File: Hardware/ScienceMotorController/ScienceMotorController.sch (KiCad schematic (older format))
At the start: 0 parts

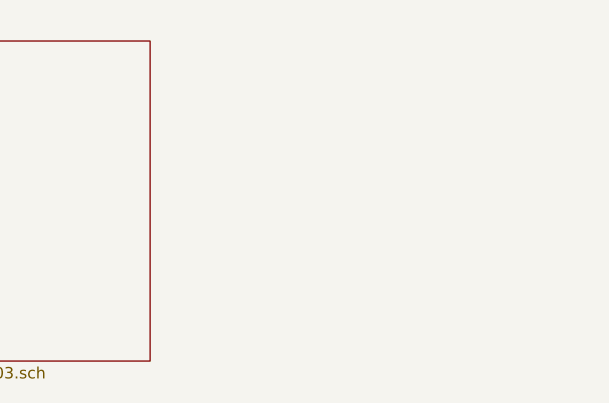
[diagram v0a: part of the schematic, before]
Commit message: Set up VNH IC's
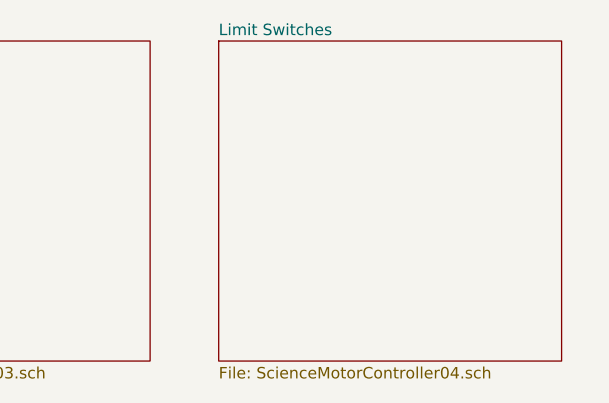
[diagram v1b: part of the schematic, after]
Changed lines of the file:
@@
 $Descr A 11000 8500
 encoding utf-8
-Sheet 1 4
+Sheet 1 10
 Title ""
 Date ""
@@
 F1 "ScienceMotorController03.sch" 50
 $EndSheet
+$Sheet
+S 6600 1050 1500 1400
+U 5F81B171
+F0 "Limit Switches" 50
+F1 "ScienceMotorController04.sch" 50
+$EndSheet
 $EndSCHEMATC

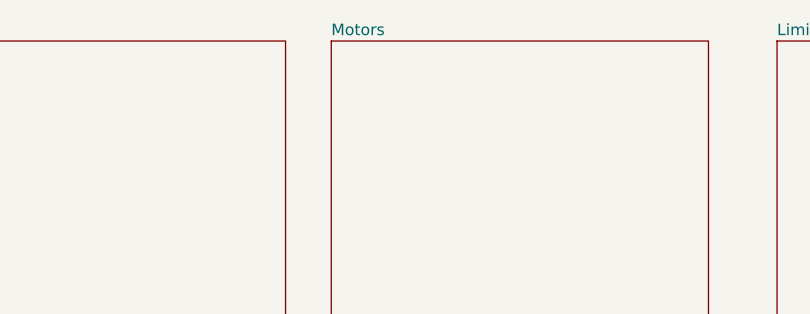
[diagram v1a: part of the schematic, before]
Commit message: Sheet titles
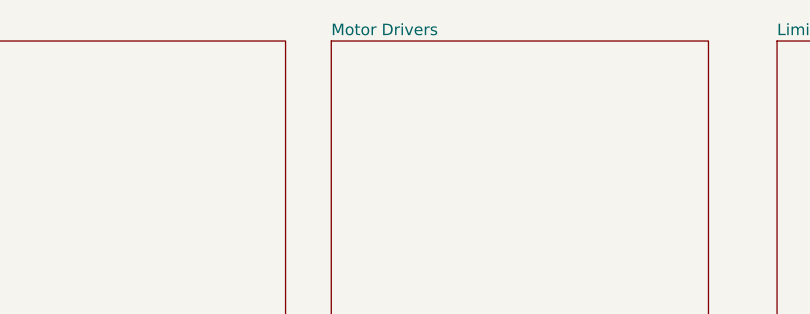
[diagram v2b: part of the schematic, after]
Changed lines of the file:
@@
 $Descr A 11000 8500
 encoding utf-8
-Sheet 1 10
+Sheet 1 11
 Title ""
 Date ""
@@
 S 4650 1050 1650 1400
 U 5F7D111E
-F0 "Motors" 50
+F0 "Motor Drivers" 50
 F1 "ScienceMotorController03.sch" 50
 $EndSheet

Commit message: schematic review
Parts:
- added Conn? (x2): AndersonPP, symbol MRDT_Connectors:AndersonPP
- added D?: LED, symbol Device:LED
- added R?: 1.2k, symbol Device:R_Small
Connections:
- new net: D?.2 (A), R?.1
- new net +12VA: Conn?.3 (V+Act), R?.2
- new net GND: Conn?.1 (GND), D?.1 (K)
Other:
- note added: "Orange"
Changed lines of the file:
@@
 $Descr A 11000 8500
 encoding utf-8
-Sheet 1 11
+Sheet 1 10
 Title ""
 Date ""
@@
 $EndDescr
 $Sheet
-S 1100 1050 1600 1400
+S 2500 900  1600 1400
 U 5F6E1E86
 F0 "Power" 50
 F1 "ScienceMotorController01.sch" 50
+F2 "12VA" I L 2500 1050 50
+F3 "3.3VA" O R 4100 1050 50
 $EndSheet
 $Sheet
-S 2800 1050 1650 1400
+S 4350 900  1650 1400
 U 5F7148FA
 F0 "Tiva" 39
 F1 "ScienceMotorController02.sch" 39
+F2 "3.3VA" I L 4350 1050 50
 $EndSheet
 $Sheet
-S 4650 1050 1650 1400
-U 5F7D111E
-F0 "Motor Drivers" 50
-F1 "ScienceMotorController03.sch" 50
-$EndSheet
-$Sheet
-S 6600 1050 1500 1400
+S 8100 900  1500 1400
 U 5F81B171
 F0 "Limit Switches" 50
 F1 "ScienceMotorController04.sch" 50
 $EndSheet
+$Comp
+L MRDT_Connectors:AndersonPP Conn?
+U 3 1 5F8E3C0A
+P 650 1400
+AR Path="/5F6E1E86/5F8E3C0A" Ref="Conn?"  Part="3"
+AR Path="/5F8E3C0A" Ref="Conn?"  Part="3"
+F 0 "Conn?" H 858 1787 60  0000 C CNN
+F 1 "AndersonPP" H 858 1681 60  0000 C CNN
+F 2 "" H 500 850 60  0001 C CNN
+F 3 "" H 500 850 60  0001 C CNN
+	3    650  1400
+	1    0    0    -1
+$EndComp
+Wire Wire Line
+	1050 1300 1200 1300
+$Comp
+L power:+12VA #PWR?
+U 1 1 5F8E3C12
+P 1200 1000
+AR Path="/5F6E1E86/5F8E3C12" Ref="#PWR?"  Part="1"
+AR Path="/5F8E3C12" Ref="#PWR?"  Part="1"
+F 0 "#PWR?" H 1200 850 50  0001 C CNN
+F 1 "+12VA" H 1215 1173 50  0000 C CNN
+F 2 "" H 1200 1000 50  0001 C CNN
+F 3 "" H 1200 1000 50  0001 C CNN
+	1    1200 1000
+	1    0    0    -1
+$EndComp
+$Comp
+L Device:LED D?
+U 1 1 5F8E3C18
+P 1700 1400
+AR Path="/5F6E1E86/5F8E3C18" Ref="D?"  Part="1"
+AR Path="/5F8E3C18" Ref="D?"  Part="1"
+F 0 "D?" H 1700 1200 50  0000 C CNN
+F 1 "LED" H 1700 1300 50  0000 C CNN
+F 2 "" H 1700 1400 50  0001 C CNN
+F 3 "~" H 1700 1400 50  0001 C CNN
+	1    1700 1400
+	-1   0    0    1
+$EndComp
+Wire Wire Line
+	1200 1400 1200 1300
+Connection ~ 1200 1300
+$Comp
+L Device:R_Small R?
+U 1 1 5F8E3C20
+P 1300 1400
+AR Path="/5F6E1E86/5F8E3C20" Ref="R?"  Part="1"
+AR Path="/5F8E3C20" Ref="R?"  Part="1"
+F 0 "R?" V 1104 1400 50  0000 C CNN
+F 1 "1.2k" V 1195 1400 50  0000 C CNN
+F 2 "" H 1300 1400 50  0001 C CNN
+F 3 "~" H 1300 1400 50  0001 C CNN
+	1    1300 1400
+	0    1    1    0
+$EndComp
+Wire Wire Line
+	1400 1400 1550 1400
+$Comp
+L power:GND #PWR?
+U 1 1 5F8E3C27
+P 1950 1450
+AR Path="/5F6E1E86/5F8E3C27" Ref="#PWR?"  Part="1"
+AR Path="/5F8E3C27" Ref="#PWR?"  Part="1"
+F 0 "#PWR?" H 1950 1200 50  0001 C CNN
+F 1 "GND" H 1955 1277 50  0000 C CNN
+F 2 "" H 1950 1450 50  0001 C CNN
+F 3 "" H 1950 1450 50  0001 C CNN
+	1    1950 1450
+	1    0    0    -1
+$EndComp
+Wire Wire Line
+	1850 1400 1950 1400
+Wire Wire Line
+	1950 1400 1950 1450
+Text Notes 1600 1500 0    50   ~ 0
+Orange
+Wire Wire Line
+	1200 1050 1200 1300
+Wire Wire Line
+	2500 1050 1200 1050
+Connection ~ 1200 1050
+Wire Wire Line
+	1200 1000 1200 1050
+$Comp
+L MRDT_Connectors:AndersonPP Conn?
+U 1 1 5F8FDE30
+P 600 2100
+AR Path="/5F6E1E86/5F8FDE30" Ref="Conn?"  Part="1"
+AR Path="/5F8FDE30" Ref="Conn?"  Part="1"
+F 0 "Conn?" H 808 2487 60  0000 C CNN
+F 1 "AndersonPP" H 808 2381 60  0000 C CNN
+F 2 "" H 450 1550 60  0001 C CNN
+F 3 "" H 450 1550 60  0001 C CNN
+	1    600  2100
+	1    0    0    -1
+$EndComp
+$Comp
+L power:GND #PWR?
+U 1 1 5F8FDE36
+P 1150 2200
+AR Path="/5F6E1E86/5F8FDE36" Ref="#PWR?"  Part="1"
+AR Path="/5F8FDE36" Ref="#PWR?"  Part="1"
+F 0 "#PWR?" H 1150 1950 50  0001 C CNN
+F 1 "GND" H 1155 2027 50  0000 C CNN
+F 2 "" H 1150 2200 50  0001 C CNN
+F 3 "" H 1150 2200 50  0001 C CNN
+	1    1150 2200
+	1    0    0    -1
+$EndComp
+Wire Wire Line
+	1150 2200 1150 2000
+Wire Wire Line
+	1150 2000 1000 2000
+Wire Wire Line
+	4100 1050 4350 1050
+$Sheet
+S 2500 3150 1450 1300
+U 5F9082F6
+F0 "sheet5F9082EF" 39
+F1 "ScienceMotorController03a.sch" 39
+$EndSheet
+$Sheet
+S 4050 3150 1400 1300
+U 5F9082F8
+F0 "sheet5F9082F0" 39
+F1 "ScienceMotorController03b.sch" 39
+$EndSheet
+$Sheet
+S 2500 4650 1450 1200
+U 5F9082FA
+F0 "sheet5F9082F1" 39
+F1 "ScienceMotorController03c.sch" 39
+$EndSheet
+$Sheet
+S 4050 4650 1400 1200
+U 5F9082FC
+F0 "sheet5F9082F2" 39
+F1 "ScienceMotorController03d.sch" 39
+$EndSheet
+$Sheet
+S 2500 6000 1450 1150
+U 5F9082FE
+F0 "sheet5F9082F3" 39
+F1 "ScienceMotorController03e.sch" 39
+$EndSheet
+$Sheet
+S 4050 6000 1400 1150
+U 5F908300
+F0 "sheet5F9082F4" 39
+F1 "ScienceMotorController03f.sch" 39
+$EndSheet
 $EndSCHEMATC

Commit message: made some more hierarchal changes
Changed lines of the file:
@@
 $EndSheet
 $Sheet
-S 8100 900  1500 1400
+S 4350 2500 1500 1400
 U 5F81B171
 F0 "Limit Switches" 50
 F1 "ScienceMotorController04.sch" 50
+F2 "3.3VA" I L 4350 2700 50
 $EndSheet
 $Comp
@@
 	1150 2000 1000 2000
 Wire Wire Line
-	4100 1050 4350 1050
+	4100 1050 4200 1050
 $Sheet
-S 2500 3150 1450 1300
+S 11700 3550 1450 1300
 U 5F9082F6
 F0 "sheet5F9082EF" 39
@@
 $EndSheet
 $Sheet
-S 4050 3150 1400 1300
+S 13250 3550 1400 1300
 U 5F9082F8
 F0 "sheet5F9082F0" 39
@@
 $EndSheet
 $Sheet
-S 2500 4650 1450 1200
+S 11700 5050 1450 1200
 U 5F9082FA
 F0 "sheet5F9082F1" 39
@@
 $EndSheet
 $Sheet
-S 4050 4650 1400 1200
+S 13250 5050 1400 1200
 U 5F9082FC
 F0 "sheet5F9082F2" 39
@@
 $EndSheet
 $Sheet
-S 2500 6000 1450 1150
+S 11700 6400 1450 1150
 U 5F9082FE
 F0 "sheet5F9082F3" 39
@@
 $EndSheet
 $Sheet
-S 4050 6000 1400 1150
+S 13250 6400 1400 1150
 U 5F908300
 F0 "sheet5F9082F4" 39
 F1 "ScienceMotorController03f.sch" 39
 $EndSheet
+Wire Wire Line
+	4350 2700 4200 2700
+Wire Wire Line
+	4200 2700 4200 1050
+Connection ~ 4200 1050
+Wire Wire Line
+	4200 1050 4350 1050
 $EndSCHEMATC

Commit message: fixed hierarchical
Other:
- moved on the sheet: Conn?A, Conn?C, D?, R?
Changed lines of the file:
@@
 $Descr A 11000 8500
 encoding utf-8
-Sheet 1 10
+Sheet 1 11
 Title ""
 Date ""
@@
 $EndDescr
 $Sheet
-S 2500 900  1600 1400
+S 4350 3300 1600 1400
 U 5F6E1E86
 F0 "Power" 50
 F1 "ScienceMotorController01.sch" 50
-F2 "12VA" I L 2500 1050 50
-F3 "3.3VA" O R 4100 1050 50
+F2 "12VA" I L 4350 3450 50
+F3 "3.3VA" O R 5950 3450 50
 $EndSheet
 $Sheet
-S 4350 900  1650 1400
+S 6200 3300 1650 1400
 U 5F7148FA
 F0 "Tiva" 39
 F1 "ScienceMotorController02.sch" 39
-F2 "3.3VA" I L 4350 1050 50
-$EndSheet
-$Sheet
-S 4350 2500 1500 1400
-U 5F81B171
-F0 "Limit Switches" 50
-F1 "ScienceMotorController04.sch" 50
-F2 "3.3VA" I L 4350 2700 50
+F2 "3.3VA" I L 6200 3450 50
 $EndSheet
 $Comp
 L MRDT_Connectors:AndersonPP Conn?
 U 3 1 5F8E3C0A
-P 650 1400
+P 2500 3800
 AR Path="/5F6E1E86/5F8E3C0A" Ref="Conn?"  Part="3"
 AR Path="/5F8E3C0A" Ref="Conn?"  Part="3"
-F 0 "Conn?" H 858 1787 60  0000 C CNN
-F 1 "AndersonPP" H 858 1681 60  0000 C CNN
-F 2 "" H 500 850 60  0001 C CNN
-F 3 "" H 500 850 60  0001 C CNN
-	3    650  1400
+F 0 "Conn?" H 2708 4187 60  0000 C CNN
+F 1 "AndersonPP" H 2708 4081 60  0000 C CNN
+F 2 "" H 2350 3250 60  0001 C CNN
+F 3 "" H 2350 3250 60  0001 C CNN
+	3    2500 3800
 	1    0    0    -1
 $EndComp
 Wire Wire Line
-	1050 1300 1200 1300
+	2900 3700 3050 3700
 $Comp
 L power:+12VA #PWR?
 U 1 1 5F8E3C12
-P 1200 1000
+P 3050 3400
 AR Path="/5F6E1E86/5F8E3C12" Ref="#PWR?"  Part="1"
 AR Path="/5F8E3C12" Ref="#PWR?"  Part="1"
-F 0 "#PWR?" H 1200 850 50  0001 C CNN
-F 1 "+12VA" H 1215 1173 50  0000 C CNN
-F 2 "" H 1200 1000 50  0001 C CNN
-F 3 "" H 1200 1000 50  0001 C CNN
-	1    1200 1000
+F 0 "#PWR?" H 3050 3250 50  0001 C CNN
+F 1 "+12VA" H 3065 3573 50  0000 C CNN
+F 2 "" H 3050 3400 50  0001 C CNN
+F 3 "" H 3050 3400 50  0001 C CNN
+	1    3050 3400
 	1    0    0    -1
 $EndComp
@@
 L Device:LED D?
 U 1 1 5F8E3C18
-P 1700 1400
+P 3550 3800
 AR Path="/5F6E1E86/5F8E3C18" Ref="D?"  Part="1"
 AR Path="/5F8E3C18" Ref="D?"  Part="1"
-F 0 "D?" H 1700 1200 50  0000 C CNN
-F 1 "LED" H 1700 1300 50  0000 C CNN
-F 2 "" H 1700 1400 50  0001 C CNN
-F 3 "~" H 1700 1400 50  0001 C CNN
-	1    1700 1400
+F 0 "D?" H 3550 3600 50  0000 C CNN
+F 1 "LED" H 3550 3700 50  0000 C CNN
+F 2 "" H 3550 3800 50  0001 C CNN
+F 3 "~" H 3550 3800 50  0001 C CNN
+	1    3550 3800
 	-1   0    0    1
 $EndComp
 Wire Wire Line
-	1200 1400 1200 1300
-Connection ~ 1200 1300
+	3050 3800 3050 3700
+Connection ~ 3050 3700
 $Comp
 L Device:R_Small R?
 U 1 1 5F8E3C20
-P 1300 1400
+P 3150 3800
 AR Path="/5F6E1E86/5F8E3C20" Ref="R?"  Part="1"
 AR Path="/5F8E3C20" Ref="R?"  Part="1"
-F 0 "R?" V 1104 1400 50  0000 C CNN
-F 1 "1.2k" V 1195 1400 50  0000 C CNN
-F 2 "" H 1300 1400 50  0001 C CNN
-F 3 "~" H 1300 1400 50  0001 C CNN
-	1    1300 1400
+F 0 "R?" V 2954 3800 50  0000 C CNN
+F 1 "1.2k" V 3045 3800 50  0000 C CNN
+F 2 "" H 3150 3800 50  0001 C CNN
+F 3 "~" H 3150 3800 50  0001 C CNN
+	1    3150 3800
 	0    1    1    0
 $EndComp
 Wire Wire Line
-	1400 1400 1550 1400
+	3250 3800 3400 3800
 $Comp
 L power:GND #PWR?
 U 1 1 5F8E3C27
-P 1950 1450
+P 3800 3850
 AR Path="/5F6E1E86/5F8E3C27" Ref="#PWR?"  Part="1"
 AR Path="/5F8E3C27" Ref="#PWR?"  Part="1"
-F 0 "#PWR?" H 1950 1200 50  0001 C CNN
-F 1 "GND" H 1955 1277 50  0000 C CNN
-F 2 "" H 1950 1450 50  0001 C CNN
-F 3 "" H 1950 1450 50  0001 C CNN
-	1    1950 1450
+F 0 "#PWR?" H 3800 3600 50  0001 C CNN
+F 1 "GND" H 3805 3677 50  0000 C CNN
+F 2 "" H 3800 3850 50  0001 C CNN
+F 3 "" H 3800 3850 50  0001 C CNN
+	1    3800 3850
 	1    0    0    -1
 $EndComp
 Wire Wire Line
-	1850 1400 1950 1400
+	3700 3800 3800 3800
 Wire Wire Line
-	1950 1400 1950 1450
-Text Notes 1600 1500 0    50   ~ 0
+	3800 3800 3800 3850
+Text Notes 3450 3900 0    50   ~ 0
 Orange
 Wire Wire Line
-	1200 1050 1200 1300
+	3050 3450 3050 3700
 Wire Wire Line
-	2500 1050 1200 1050
-Connection ~ 1200 1050
+	4350 3450 3050 3450
+Connection ~ 3050 3450
 Wire Wire Line
-	1200 1000 1200 1050
+	3050 3400 3050 3450
 $Comp
 L MRDT_Connectors:AndersonPP Conn?
 U 1 1 5F8FDE30
-P 600 2100
+P 2500 4300
 AR Path="/5F6E1E86/5F8FDE30" Ref="Conn?"  Part="1"
 AR Path="/5F8FDE30" Ref="Conn?"  Part="1"
-F 0 "Conn?" H 808 2487 60  0000 C CNN
-F 1 "AndersonPP" H 808 2381 60  0000 C CNN
-F 2 "" H 450 1550 60  0001 C CNN
-F 3 "" H 450 1550 60  0001 C CNN
-	1    600  2100
+F 0 "Conn?" H 2708 4687 60  0000 C CNN
+F 1 "AndersonPP" H 2708 4581 60  0000 C CNN
+F 2 "" H 2350 3750 60  0001 C CNN
+F 3 "" H 2350 3750 60  0001 C CNN
+	1    2500 4300
 	1    0    0    -1
 $EndComp
@@
 L power:GND #PWR?
 U 1 1 5F8FDE36
-P 1150 2200
+P 3050 4400
 AR Path="/5F6E1E86/5F8FDE36" Ref="#PWR?"  Part="1"
 AR Path="/5F8FDE36" Ref="#PWR?"  Part="1"
-F 0 "#PWR?" H 1150 1950 50  0001 C CNN
-F 1 "GND" H 1155 2027 50  0000 C CNN
-F 2 "" H 1150 2200 50  0001 C CNN
-F 3 "" H 1150 2200 50  0001 C CNN
-	1    1150 2200
+F 0 "#PWR?" H 3050 4150 50  0001 C CNN
+F 1 "GND" H 3055 4227 50  0000 C CNN
+F 2 "" H 3050 4400 50  0001 C CNN
+F 3 "" H 3050 4400 50  0001 C CNN
+	1    3050 4400
 	1    0    0    -1
 $EndComp
 Wire Wire Line
-	1150 2200 1150 2000
+	3050 4400 3050 4200
 Wire Wire Line
-	1150 2000 1000 2000
+	3050 4200 2900 4200
 Wire Wire Line
-	4100 1050 4200 1050
-$Sheet
-S 11700 3550 1450 1300
-U 5F9082F6
-F0 "sheet5F9082EF" 39
-F1 "ScienceMotorController03a.sch" 39
-$EndSheet
-$Sheet
-S 13250 3550 1400 1300
-U 5F9082F8
-F0 "sheet5F9082F0" 39
-F1 "ScienceMotorController03b.sch" 39
-$EndSheet
-$Sheet
-S 11700 5050 1450 1200
-U 5F9082FA
-F0 "sheet5F9082F1" 39
-F1 "ScienceMotorController03c.sch" 39
-$EndSheet
-$Sheet
-S 13250 5050 1400 1200
-U 5F9082FC
-F0 "sheet5F9082F2" 39
-F1 "ScienceMotorController03d.sch" 39
-$EndSheet
-$Sheet
-S 11700 6400 1450 1150
-U 5F9082FE
-F0 "sheet5F9082F3" 39
-F1 "ScienceMotorController03e.sch" 39
-$EndSheet
-$Sheet
-S 13250 6400 1400 1150
-U 5F908300
-F0 "sheet5F9082F4" 39
-F1 "ScienceMotorController03f.sch" 39
-$EndSheet
-Wire Wire Line
-	4350 2700 4200 2700
-Wire Wire Line
-	4200 2700 4200 1050
-Connection ~ 4200 1050
-Wire Wire Line
-	4200 1050 4350 1050
+	5950 3450 6200 3450
 $EndSCHEMATC

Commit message: added logic line
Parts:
- added Conn?: AndersonPP, symbol MRDT_Connectors:AndersonPP
- added D?: LED, symbol Device:LED
- added R?: 1.2k, symbol Device:R_Small
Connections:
- net GND: now also D?.1 (K)
- new net: D?.2 (A), R?.1
- new net Power/12V: Conn?.2 (V+Log), R?.2
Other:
- moved on the sheet: Conn?A
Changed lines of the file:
@@
 F0 "Power" 50
 F1 "ScienceMotorController01.sch" 50
-F2 "12VA" I L 4350 3450 50
-F3 "3.3VA" O R 5950 3450 50
+F2 "12V" I L 4350 4250 50
+F3 "3.3V" O R 5950 3450 50
 $EndSheet
 $Sheet
@@
 F0 "Tiva" 39
 F1 "ScienceMotorController02.sch" 39
-F2 "3.3VA" I L 6200 3450 50
+F2 "3.3V" I L 6200 3450 50
 $EndSheet
 $Comp
@@
 AR Path="/5F8E3C20" Ref="R?"  Part="1"
 F 0 "R?" V 2954 3800 50  0000 C CNN
-F 1 "1.2k" V 3045 3800 50  0000 C CNN
+F 1 "1.2k" V 3150 3800 39  0000 C CNN
 F 2 "" H 3150 3800 50  0001 C CNN
 F 3 "~" H 3150 3800 50  0001 C CNN
@@
 Text Notes 3450 3900 0    50   ~ 0
 Orange
-Wire Wire Line
-	3050 3450 3050 3700
-Wire Wire Line
-	4350 3450 3050 3450
-Connection ~ 3050 3450
-Wire Wire Line
-	3050 3400 3050 3450
 $Comp
 L MRDT_Connectors:AndersonPP Conn?
 U 1 1 5F8FDE30
-P 2500 4300
+P 2500 4950
 AR Path="/5F6E1E86/5F8FDE30" Ref="Conn?"  Part="1"
 AR Path="/5F8FDE30" Ref="Conn?"  Part="1"
-F 0 "Conn?" H 2708 4687 60  0000 C CNN
-F 1 "AndersonPP" H 2708 4581 60  0000 C CNN
-F 2 "" H 2350 3750 60  0001 C CNN
-F 3 "" H 2350 3750 60  0001 C CNN
-	1    2500 4300
+F 0 "Conn?" H 2708 5337 60  0000 C CNN
+F 1 "AndersonPP" H 2708 5231 60  0000 C CNN
+F 2 "" H 2350 4400 60  0001 C CNN
+F 3 "" H 2350 4400 60  0001 C CNN
+	1    2500 4950
 	1    0    0    -1
 $EndComp
@@
 L power:GND #PWR?
 U 1 1 5F8FDE36
-P 3050 4400
+P 3050 5050
 AR Path="/5F6E1E86/5F8FDE36" Ref="#PWR?"  Part="1"
 AR Path="/5F8FDE36" Ref="#PWR?"  Part="1"
-F 0 "#PWR?" H 3050 4150 50  0001 C CNN
-F 1 "GND" H 3055 4227 50  0000 C CNN
-F 2 "" H 3050 4400 50  0001 C CNN
-F 3 "" H 3050 4400 50  0001 C CNN
-	1    3050 4400
+F 0 "#PWR?" H 3050 4800 50  0001 C CNN
+F 1 "GND" H 3055 4877 50  0000 C CNN
+F 2 "" H 3050 5050 50  0001 C CNN
+F 3 "" H 3050 5050 50  0001 C CNN
+	1    3050 5050
 	1    0    0    -1
 $EndComp
 Wire Wire Line
-	3050 4400 3050 4200
+	3050 5050 3050 4850
 Wire Wire Line
-	3050 4200 2900 4200
+	3050 4850 2900 4850
 Wire Wire Line
 	5950 3450 6200 3450
+$Comp
+L MRDT_Connectors:AndersonPP Conn?
+U 2 1 5FA9F774
+P 2500 4350
+F 0 "Conn?" H 2708 4737 60  0000 C CNN
+F 1 "AndersonPP" H 2708 4631 60  0000 C CNN
+F 2 "" H 2350 3800 60  0001 C CNN
+F 3 "" H 2350 3800 60  0001 C CNN
+	2    2500 4350
+	1    0    0    -1
+$EndComp
+Wire Wire Line
+	2900 4250 3150 4250
+Connection ~ 3150 4250
+Wire Wire Line
+	3150 4250 4350 4250
+Wire Wire Line
+	3150 4450 3200 4450
+Wire Wire Line
+	3150 4250 3150 4450
+$Comp
+L Device:R_Small R?
+U 1 1 5FAA2CAF
+P 3300 4450
+AR Path="/5F6E1E86/5FAA2CAF" Ref="R?"  Part="1"
+AR Path="/5FAA2CAF" Ref="R?"  Part="1"
+F 0 "R?" V 3200 4450 50  0000 C CNN
+F 1 "1.2k" V 3300 4450 39  0000 C CNN
+F 2 "" H 3300 4450 50  0001 C CNN
+F 3 "~" H 3300 4450 50  0001 C CNN
+	1    3300 4450
+	0    1    1    0
+$EndComp
+$Comp
+L Device:LED D?
+U 1 1 5FAA3A99
+P 3600 4450
+AR Path="/5F6E1E86/5FAA3A99" Ref="D?"  Part="1"
+AR Path="/5FAA3A99" Ref="D?"  Part="1"
+F 0 "D?" H 3700 4400 50  0000 C CNN
+F 1 "LED" H 3600 4350 50  0000 C CNN
+F 2 "" H 3600 4450 50  0001 C CNN
+F 3 "~" H 3600 4450 50  0001 C CNN
+	1    3600 4450
+	-1   0    0    1
+$EndComp
+Wire Wire Line
+	3400 4450 3450 4450
+$Comp
+L power:GND #PWR?
+U 1 1 5FAA490A
+P 3850 4450
+AR Path="/5F6E1E86/5FAA490A" Ref="#PWR?"  Part="1"
+AR Path="/5FAA490A" Ref="#PWR?"  Part="1"
+F 0 "#PWR?" H 3850 4200 50  0001 C CNN
+F 1 "GND" H 3855 4277 50  0000 C CNN
+F 2 "" H 3850 4450 50  0001 C CNN
+F 3 "" H 3850 4450 50  0001 C CNN
+	1    3850 4450
+	1    0    0    -1
+$EndComp
+Wire Wire Line
+	3750 4450 3850 4450
+Wire Wire Line
+	3050 3400 3050 3700
 $EndSCHEMATC

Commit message: annotated
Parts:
- gave numbers to parts that had none: 5
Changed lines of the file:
@@
 P 2500 3800
 AR Path="/5F6E1E86/5F8E3C0A" Ref="Conn?"  Part="3"
-AR Path="/5F8E3C0A" Ref="Conn?"  Part="3"
-F 0 "Conn?" H 2708 4187 60  0000 C CNN
+AR Path="/5F8E3C0A" Ref="Conn1"  Part="3"
+F 0 "Conn1" H 2708 4187 60  0000 C CNN
 F 1 "AndersonPP" H 2708 4081 60  0000 C CNN
 F 2 "" H 2350 3250 60  0001 C CNN
@@
 P 3050 3400
 AR Path="/5F6E1E86/5F8E3C12" Ref="#PWR?"  Part="1"
-AR Path="/5F8E3C12" Ref="#PWR?"  Part="1"
-F 0 "#PWR?" H 3050 3250 50  0001 C CNN
+AR Path="/5F8E3C12" Ref="#PWR01"  Part="1"
+F 0 "#PWR01" H 3050 3250 50  0001 C CNN
 F 1 "+12VA" H 3065 3573 50  0000 C CNN
 F 2 "" H 3050 3400 50  0001 C CNN
@@
 P 3550 3800
 AR Path="/5F6E1E86/5F8E3C18" Ref="D?"  Part="1"
-AR Path="/5F8E3C18" Ref="D?"  Part="1"
-F 0 "D?" H 3550 3600 50  0000 C CNN
+AR Path="/5F8E3C18" Ref="D1"  Part="1"
+F 0 "D1" H 3550 3600 50  0000 C CNN
 F 1 "LED" H 3550 3700 50  0000 C CNN
 F 2 "" H 3550 3800 50  0001 C CNN
@@
 P 3150 3800
 AR Path="/5F6E1E86/5F8E3C20" Ref="R?"  Part="1"
-AR Path="/5F8E3C20" Ref="R?"  Part="1"
-F 0 "R?" V 2954 3800 50  0000 C CNN
+AR Path="/5F8E3C20" Ref="R1"  Part="1"
+F 0 "R1" V 2954 3800 50  0000 C CNN
 F 1 "1.2k" V 3150 3800 39  0000 C CNN
 F 2 "" H 3150 3800 50  0001 C CNN
@@
 P 3800 3850
 AR Path="/5F6E1E86/5F8E3C27" Ref="#PWR?"  Part="1"
-AR Path="/5F8E3C27" Ref="#PWR?"  Part="1"
-F 0 "#PWR?" H 3800 3600 50  0001 C CNN
+AR Path="/5F8E3C27" Ref="#PWR03"  Part="1"
+F 0 "#PWR03" H 3800 3600 50  0001 C CNN
 F 1 "GND" H 3805 3677 50  0000 C CNN
 F 2 "" H 3800 3850 50  0001 C CNN
@@
 P 2500 4950
 AR Path="/5F6E1E86/5F8FDE30" Ref="Conn?"  Part="1"
-AR Path="/5F8FDE30" Ref="Conn?"  Part="1"
-F 0 "Conn?" H 2708 5337 60  0000 C CNN
+AR Path="/5F8FDE30" Ref="Conn1"  Part="1"
+F 0 "Conn1" H 2708 5337 60  0000 C CNN
 F 1 "AndersonPP" H 2708 5231 60  0000 C CNN
 F 2 "" H 2350 4400 60  0001 C CNN
@@
 P 3050 5050
 AR Path="/5F6E1E86/5F8FDE36" Ref="#PWR?"  Part="1"
-AR Path="/5F8FDE36" Ref="#PWR?"  Part="1"
-F 0 "#PWR?" H 3050 4800 50  0001 C CNN
+AR Path="/5F8FDE36" Ref="#PWR02"  Part="1"
+F 0 "#PWR02" H 3050 4800 50  0001 C CNN
 F 1 "GND" H 3055 4877 50  0000 C CNN
 F 2 "" H 3050 5050 50  0001 C CNN
@@
 	5950 3450 6200 3450
 $Comp
-L MRDT_Connectors:AndersonPP Conn?
+L MRDT_Connectors:AndersonPP Conn1
 U 2 1 5FA9F774
 P 2500 4350
-F 0 "Conn?" H 2708 4737 60  0000 C CNN
+F 0 "Conn1" H 2708 4737 60  0000 C CNN
 F 1 "AndersonPP" H 2708 4631 60  0000 C CNN
 F 2 "" H 2350 3800 60  0001 C CNN
@@
 P 3300 4450
 AR Path="/5F6E1E86/5FAA2CAF" Ref="R?"  Part="1"
-AR Path="/5FAA2CAF" Ref="R?"  Part="1"
-F 0 "R?" V 3200 4450 50  0000 C CNN
+AR Path="/5FAA2CAF" Ref="R2"  Part="1"
+F 0 "R2" V 3200 4450 50  0000 C CNN
 F 1 "1.2k" V 3300 4450 39  0000 C CNN
 F 2 "" H 3300 4450 50  0001 C CNN
@@
 P 3600 4450
 AR Path="/5F6E1E86/5FAA3A99" Ref="D?"  Part="1"
-AR Path="/5FAA3A99" Ref="D?"  Part="1"
-F 0 "D?" H 3700 4400 50  0000 C CNN
+AR Path="/5FAA3A99" Ref="D2"  Part="1"
+F 0 "D2" H 3700 4400 50  0000 C CNN
 F 1 "LED" H 3600 4350 50  0000 C CNN
 F 2 "" H 3600 4450 50  0001 C CNN
@@
 P 3850 4450
 AR Path="/5F6E1E86/5FAA490A" Ref="#PWR?"  Part="1"
-AR Path="/5FAA490A" Ref="#PWR?"  Part="1"
-F 0 "#PWR?" H 3850 4200 50  0001 C CNN
+AR Path="/5FAA490A" Ref="#PWR04"  Part="1"
+F 0 "#PWR04" H 3850 4200 50  0001 C CNN
 F 1 "GND" H 3855 4277 50  0000 C CNN
 F 2 "" H 3850 4450 50  0001 C CNN
